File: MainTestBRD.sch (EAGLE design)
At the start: 24 parts, among them J1 COMPUTER-PERIPHERAL-POWERVERT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, U1 ATMEGA128-SMD

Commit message: intermedate variant
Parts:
- R1, R2: value (none) -> 1.8k; device mbed-rlcq:R0.125W -> SparkFun-Resistors:1.8KOHM1/10W1%(0603)
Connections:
- net N$13 renamed RESET
- net LED1: now also R1.2; no longer R1.P$1
- net LED2: now also R2.2; no longer R2.P$1
- net N$2: now also R2.1; no longer R2.P$2
- net N$5: now also R1.1; no longer R1.P$2
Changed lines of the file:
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@@
 <part name="U1" library="SparkFun-DigitalIC" deviceset="ATMEGA128" device="-SMD"/>
 <part name="GND1" library="mbed-power" deviceset="GND" device=""/>
-<part name="R1" library="mbed-rlcq" deviceset="R" device="0.125W"/>
-<part name="R2" library="mbed-rlcq" deviceset="R" device="0.125W"/>
 <part name="GND3" library="mbed-power" deviceset="GND" device=""/>
 <part name="GND4" library="mbed-power" deviceset="GND" device=""/>
@@
 <part name="C9" library="SparkFun-Capacitors" deviceset="10UF-6.3V-20%(1206)" device="" value="10pF"/>
 <part name="C10" library="SparkFun-Capacitors" deviceset="10UF-6.3V-20%(1206)" device="" value="10pF"/>
+<part name="R1" library="SparkFun-Resistors" deviceset="1.8KOHM1/10W1%(0603)" device="" value="1.8k"/>
+<part name="R2" library="SparkFun-Resistors" deviceset="1.8KOHM1/10W1%(0603)" device="" value="1.8k"/>
 </parts>
 <sheets>
@@
 <instance part="U1" gate="G$1" x="177.8" y="71.12"/>
 <instance part="GND1" gate="1" x="55.88" y="12.7"/>
-<instance part="R1" gate="G$1" x="81.28" y="50.8"/>
-<instance part="R2" gate="G$1" x="81.28" y="33.02"/>
 <instance part="GND3" gate="1" x="205.74" y="7.62"/>
 <instance part="GND4" gate="1" x="134.62" y="91.44"/>
@@
 <instance part="C9" gate="G$1" x="236.22" y="86.36" rot="R90"/>
 <instance part="C10" gate="G$1" x="236.22" y="96.52" rot="R90"/>
+<instance part="R1" gate="G$1" x="81.28" y="50.8" rot="R180"/>
+<instance part="R2" gate="G$1" x="81.28" y="33.02" rot="R180"/>
 </instances>
 <busses>
@@
 <segment>
 <pinref part="U$1" gate="G$1" pin="PIO5"/>
-<pinref part="R1" gate="G$1" pin="P$1"/>
 <wire x1="76.2" y1="50.8" x2="50.8" y2="50.8" width="0.1524" layer="91"/>
+<pinref part="R1" gate="G$1" pin="2"/>
 </segment>
 </net>
 <net name="N$5" class="0">
 <segment>
-<pinref part="R1" gate="G$1" pin="P$2"/>
 <wire x1="86.36" y1="50.8" x2="88.9" y2="50.8" width="0.1524" layer="91"/>
 <pinref part="LED1" gate="G$1" pin="C"/>
+<pinref part="R1" gate="G$1" pin="1"/>
 </segment>
 </net>
 <net name="N$2" class="0">
 <segment>
-<pinref part="R2" gate="G$1" pin="P$2"/>
 <wire x1="88.9" y1="33.02" x2="86.36" y2="33.02" width="0.1524" layer="91"/>
 <pinref part="LED2" gate="G$1" pin="C"/>
+<pinref part="R2" gate="G$1" pin="1"/>
 </segment>
 </net>
@@
 <wire x1="50.8" y1="43.18" x2="53.34" y2="43.18" width="0.1524" layer="91"/>
 <wire x1="53.34" y1="43.18" x2="53.34" y2="33.02" width="0.1524" layer="91"/>
-<pinref part="R2" gate="G$1" pin="P$1"/>
 <wire x1="53.34" y1="33.02" x2="76.2" y2="33.02" width="0.1524" layer="91"/>
+<pinref part="R2" gate="G$1" pin="2"/>
 </segment>
 </net>
@@
 </segment>
 </net>
-<net name="N$13" class="0">
+<net name="RESET" class="0">
 <segment>
 <pinref part="S1" gate="S" pin="4"/>

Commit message: other pinouts
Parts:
- removed J1: COMPUTER-PERIPHERAL-POWERVERTICAL, SparkFun-Connectors:COMPUTER-PERIPHERAL-POWERVERTICAL
- removed U$2: JTAGICE3-CONNECTOR100MIL-SMD, con-jtagice3:JTAGICE3-CONNECTOR100MIL-SMD
- added JP1: M05X2PTH, SparkFun-Connectors:M05X2PTH
- added U$3: JTAGICE3-CONNECTOR50MIL-THT, con-jtagice3:JTAGICE3-CONNECTOR50MIL-THT
- added U2: (no value), SparkFun-Connectors:USB-AB
- R3: device SparkFun-Resistors:1.8KOHM1/10W1%(0603) -> SparkFun-Resistors:3.3KOHM1/10W1%(0603)
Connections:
- new net N$10: JP1.10, U1.PE4
- new net N$11: JP1.8, U1.PE3
- new net N$12: JP1.6, U1.PE2
- new net N$13: JP1.4, U1.PE1(TXD)
- new net N$14: JP1.2, U1.PE0(RXD)
- new net N$15: JP1.9, U1.PE5
- new net N$16: JP1.7, U1.PE6
- new net N$17: JP1.5, U1.PE7
- new net N$3: R3.1, U1.PD3
- net BT_RX: no longer R3.1, U1.PD3
- net GND: now also JP1.3, U$3.GND@0, U$3.GND@1, U2.GND; no longer J1.GND
- net PF4: now also U$3.TCK; no longer U$2.TCK
- net PF5: now also U$3.TMS; no longer U$2.TMS
- net PF6: now also U$3.TDO; no longer U$2.TDO
- net PF7: now also U$3.TDI; no longer U$2.TDI
- net VCC: now also JP1.1, U$3.VTG, U2.VBUS; no longer J1.5V, U$2.VTG
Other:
- moved on the sheet: LED1, LED2, R1, R2, R3

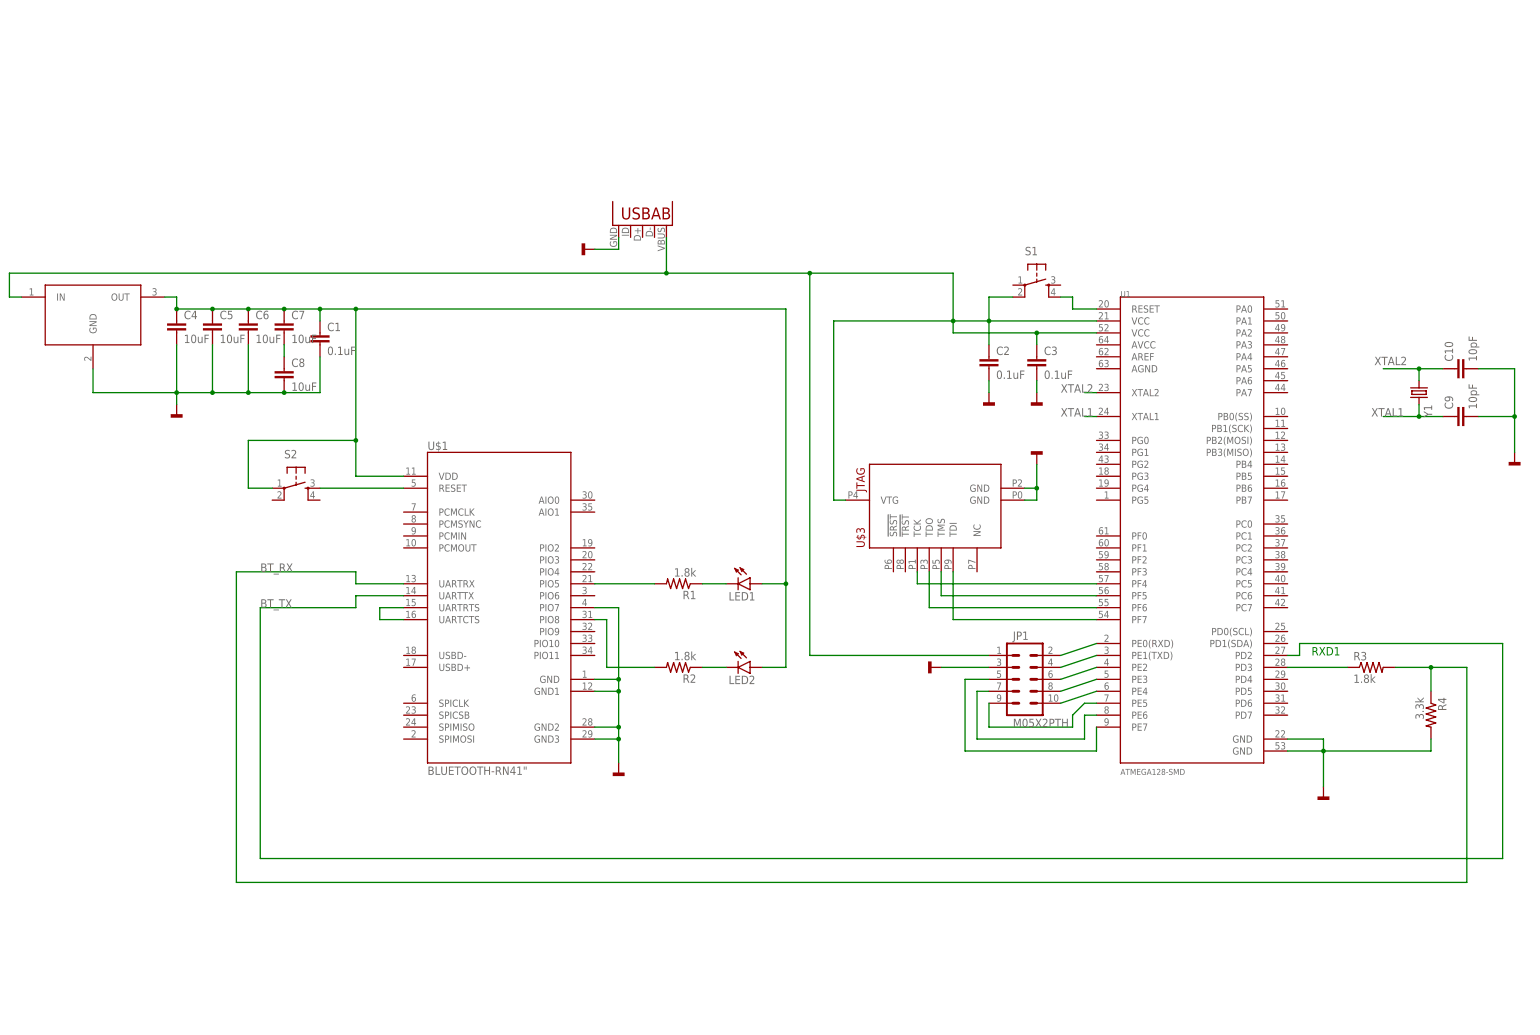
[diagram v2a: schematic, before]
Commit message: additional pin outs added
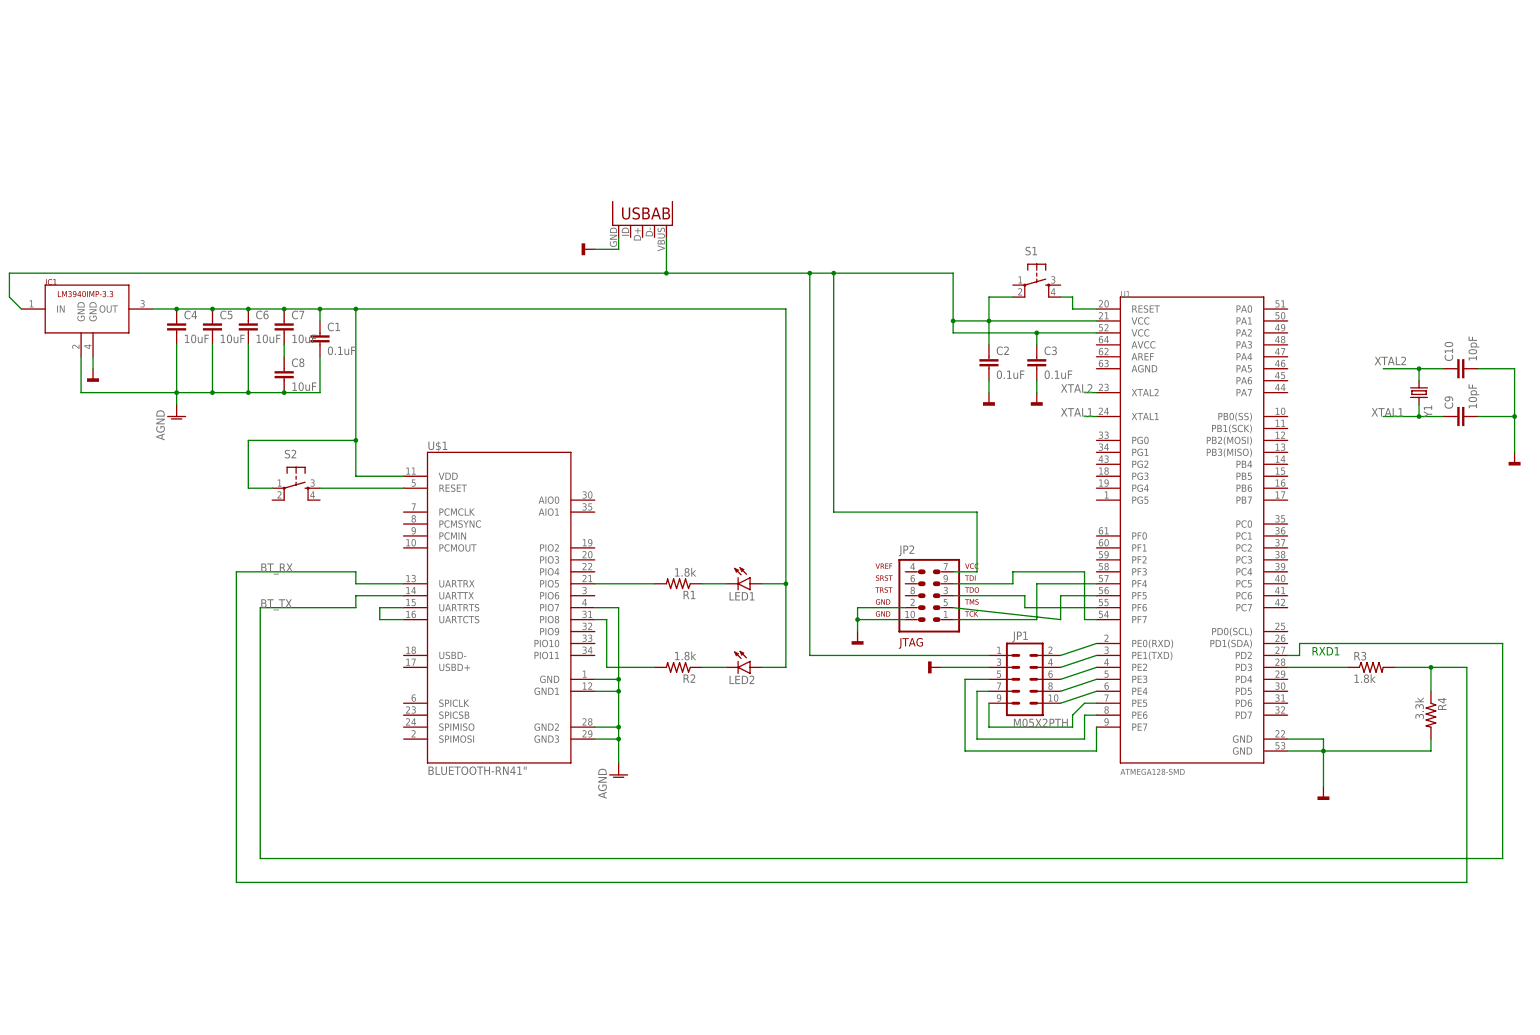
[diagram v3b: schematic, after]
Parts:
- removed IT1: LM3940IT-3.3, LM3940:LM3940IT-3.3
- removed U$3: JTAGICE3-CONNECTOR50MIL-THT, con-jtagice3:JTAGICE3-CONNECTOR50MIL-THT
- added IC1: LM3940IMP-3.3, mylib:LM3940IMP-3.3
- added JP2: AVR-JTAG-10, atmel:AVR-JTAG-10
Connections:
- removed net PF4: U$3.TCK, U1.PF4
- removed net PF5: U$3.TMS, U1.PF5
- removed net PF6: U$3.TDO, U1.PF6
- removed net PF7: U$3.TDI, U1.PF7
- new net AGND: C1.2, C4.2, C5.2, C6.2, C8.2, IC1.GND@1, U$1.GND, U$1.GND1, U$1.GND2, U$1.GND3, U$1.PIO7
- new net N$18: JP2.3, U1.PF6
- new net N$19: JP2.9, U1.PF7
- new net N$6: JP2.1, U1.PF4
- new net N$9: JP2.5, U1.PF5
- net GND: now also IC1.GND@2, JP2.10, JP2.2; no longer C1.2, C4.2, C5.2, C6.2, C8.2, IT1.GND, U$1.GND, U$1.GND1, U$1.GND2, U$1.GND3, U$1.PIO7, U$3.GND@0, U$3.GND@1
- net VCC: now also IC1.IN, JP2.7; no longer IT1.IN, U$3.VTG
- net VDD: now also IC1.OUT; no longer IT1.OUT

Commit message: new power led
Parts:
- added LED3: (no value), SparkFun-LED:LED1206
- added R5: 1.8k, SparkFun-Resistors:1.8KOHM1/10W1%(0603)
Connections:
- new net N$20: LED3.C, R5.1
- net GND: now also R5.2
- net VCC: now also LED3.A
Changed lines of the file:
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@@
 <part name="GND1" library="mbed-power" deviceset="GND" device=""/>
 <part name="JP2" library="atmel" deviceset="AVR-JTAG-10" device=""/>
+<part name="LED3" library="SparkFun-LED" deviceset="LED" device="1206"/>
+<part name="GND6" library="mbed-power" deviceset="GND" device=""/>
+<part name="R5" library="SparkFun-Resistors" deviceset="1.8KOHM1/10W1%(0603)" device="" value="1.8k"/>
 </parts>
 <sheets>
@@
 <instance part="GND1" gate="1" x="-55.88" y="96.52"/>
 <instance part="JP2" gate="G$1" x="121.92" y="48.26"/>
+<instance part="LED3" gate="G$1" x="83.82" y="121.92" rot="R180"/>
+<instance part="GND6" gate="1" x="83.82" y="137.16" rot="R180"/>
+<instance part="R5" gate="G$1" x="83.82" y="132.08" rot="R90"/>
 </instances>
 <busses>
@@
 <pinref part="GND1" gate="1" pin="GND"/>
 <wire x1="-55.88" y1="96.52" x2="-55.88" y2="99.06" width="0.1524" layer="91"/>
+</segment>
+<segment>
+<pinref part="GND6" gate="1" pin="GND"/>
+<pinref part="R5" gate="G$1" pin="2"/>
 </segment>
 </net>
@@
 <wire x1="-73.66" y1="116.84" x2="-73.66" y2="111.76" width="0.1524" layer="91"/>
 <wire x1="-73.66" y1="111.76" x2="-71.12" y2="109.22" width="0.1524" layer="91"/>
-<wire x1="66.04" y1="116.84" x2="96.52" y2="116.84" width="0.1524" layer="91"/>
+<wire x1="66.04" y1="116.84" x2="83.82" y2="116.84" width="0.1524" layer="91"/>
+<wire x1="83.82" y1="116.84" x2="96.52" y2="116.84" width="0.1524" layer="91"/>
 <wire x1="96.52" y1="116.84" x2="101.6" y2="116.84" width="0.1524" layer="91"/>
 <wire x1="101.6" y1="116.84" x2="127" y2="116.84" width="0.1524" layer="91"/>
@@
 <wire x1="132.08" y1="66.04" x2="101.6" y2="66.04" width="0.1524" layer="91"/>
 <junction x="101.6" y="116.84"/>
+<pinref part="LED3" gate="G$1" pin="A"/>
+<wire x1="83.82" y1="119.38" x2="83.82" y2="116.84" width="0.1524" layer="91"/>
+<junction x="83.82" y="116.84"/>
 </segment>
 </net>
@@
 </segment>
 </net>
+<net name="N$20" class="0">
+<segment>
+<pinref part="LED3" gate="G$1" pin="C"/>
+<pinref part="R5" gate="G$1" pin="1"/>
+</segment>
+</net>

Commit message: new usb connector
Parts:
- removed U2: (no value), SparkFun-Connectors:USB-AB
- added JP4: USB-B, SparkFun-Connectors:USBPTH
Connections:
- net GND: now also JP4.GND; no longer U2.GND
- net VCC: now also JP4.VBUS; no longer U2.VBUS
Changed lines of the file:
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@@
 <part name="R1" library="SparkFun-Resistors" deviceset="1.8KOHM1/10W1%(0603)" device="" value="1.8k"/>
 <part name="R2" library="SparkFun-Resistors" deviceset="1.8KOHM1/10W1%(0603)" device="" value="1.8k"/>
-<part name="U2" library="SparkFun-Connectors" deviceset="USB-AB" device=""/>
 <part name="GND8" library="mbed-power" deviceset="GND" device=""/>
 <part name="R3" library="SparkFun-Resistors" deviceset="3.3KOHM1/10W1%(0603)" device="" value="1.8k"/>
@@
 <part name="GND6" library="mbed-power" deviceset="GND" device=""/>
 <part name="R5" library="SparkFun-Resistors" deviceset="1.8KOHM1/10W1%(0603)" device="" value="1.8k"/>
+<part name="JP4" library="SparkFun-Connectors" deviceset="USB" device="PTH" value="USB-B"/>
 </parts>
 <sheets>
@@
 <instance part="LED2" gate="G$1" x="83.82" y="33.02" rot="R270"/>
 <instance part="S2" gate="S" x="-12.7" y="71.12"/>
-<instance part="GND2" gate="1" x="50.8" y="121.92" rot="R270"/>
+<instance part="GND2" gate="1" x="63.5" y="121.92" rot="R90"/>
 <instance part="Y1" gate="G$1" x="226.06" y="91.44" rot="R270"/>
 <instance part="GND7" gate="1" x="246.38" y="78.74"/>
@@
 <instance part="R1" gate="G$1" x="68.58" y="50.8" rot="R180"/>
 <instance part="R2" gate="G$1" x="68.58" y="33.02" rot="R180"/>
-<instance part="U2" gate="G$1" x="60.96" y="129.54" rot="R90"/>
 <instance part="GND8" gate="1" x="106.68" y="40.64"/>
 <instance part="R3" gate="G$1" x="215.9" y="33.02"/>
@@
 <instance part="GND6" gate="1" x="83.82" y="137.16" rot="R180"/>
 <instance part="R5" gate="G$1" x="83.82" y="132.08" rot="R90"/>
+<instance part="JP4" gate="G$1" x="60.96" y="127" rot="R90"/>
 </instances>
 <busses>
@@
 </segment>
 <segment>
-<wire x1="55.88" y1="121.92" x2="50.8" y2="121.92" width="0.1524" layer="91"/>
-<pinref part="GND2" gate="1" pin="GND"/>
-<pinref part="U2" gate="G$1" pin="GND"/>
-<wire x1="55.88" y1="121.92" x2="55.88" y2="124.46" width="0.1524" layer="91"/>
-</segment>
-<segment>
 <wire x1="238.76" y1="96.52" x2="246.38" y2="96.52" width="0.1524" layer="91"/>
 <pinref part="GND7" gate="1" pin="GND"/>
@@
 <pinref part="GND6" gate="1" pin="GND"/>
 <pinref part="R5" gate="G$1" pin="2"/>
+</segment>
+<segment>
+<pinref part="GND2" gate="1" pin="GND"/>
+<wire x1="63.5" y1="121.92" x2="60.96" y2="124.46" width="0.1524" layer="91"/>
+<pinref part="JP4" gate="G$1" pin="GND"/>
 </segment>
 </net>
@@
 <wire x1="-73.66" y1="116.84" x2="-73.66" y2="111.76" width="0.1524" layer="91"/>
 <wire x1="-73.66" y1="111.76" x2="-71.12" y2="109.22" width="0.1524" layer="91"/>
-<wire x1="66.04" y1="116.84" x2="83.82" y2="116.84" width="0.1524" layer="91"/>
 <wire x1="83.82" y1="116.84" x2="96.52" y2="116.84" width="0.1524" layer="91"/>
 <wire x1="96.52" y1="116.84" x2="101.6" y2="116.84" width="0.1524" layer="91"/>
@@
 <wire x1="134.62" y1="111.76" x2="134.62" y2="106.68" width="0.1524" layer="91"/>
 <wire x1="127" y1="116.84" x2="127" y2="106.68" width="0.1524" layer="91"/>
-<wire x1="-73.66" y1="116.84" x2="66.04" y2="116.84" width="0.1524" layer="91"/>
-<junction x="66.04" y="116.84"/>
+<wire x1="-73.66" y1="116.84" x2="58.42" y2="116.84" width="0.1524" layer="91"/>
 <pinref part="C2" gate="G$1" pin="1"/>
 <pinref part="C3" gate="G$1" pin="1"/>
-<pinref part="U2" gate="G$1" pin="VBUS"/>
-<wire x1="66.04" y1="116.84" x2="66.04" y2="124.46" width="0.1524" layer="91"/>
 <junction x="96.52" y="116.84"/>
+<wire x1="58.42" y1="116.84" x2="83.82" y2="116.84" width="0.1524" layer="91"/>
 <wire x1="96.52" y1="116.84" x2="96.52" y2="35.56" width="0.1524" layer="91"/>
 <wire x1="96.52" y1="35.56" x2="134.62" y2="35.56" width="0.1524" layer="91"/>
@@
 <wire x1="83.82" y1="119.38" x2="83.82" y2="116.84" width="0.1524" layer="91"/>
 <junction x="83.82" y="116.84"/>
-</segment>
-</net>
+<wire x1="58.42" y1="124.46" x2="58.42" y2="116.84" width="0.1524" layer="91"/>
+<junction x="58.42" y="116.84"/>
+<pinref part="JP4" gate="G$1" pin="VBUS"/>
+</segment>
+</net>

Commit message: новая версия
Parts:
- removed LED1, LED2: (no value), SparkFun-LED:LED1206
- removed R1, R2: 1.8k, SparkFun-Resistors:1.8KOHM1/10W1%(0603)
- removed S2: (no value), SparkFun-Electromechanical:TAC_SWITCHPTH
- removed U1: ATMEGA128-SMD, SparkFun-DigitalIC:ATMEGA128-SMD
- added BAT1: (no value), special:BATTERY
- added BLUE, GREEN, RED: (no value), SparkFun-LED:LED1206
- added C11: 10uF, SparkFun-Capacitors:10UF-6.3V-20%(1206)
- added IC2: AT90CAN128, at90can128:AT90CAN128
- added R6, R7, R8: 330R, SparkFun-Resistors:1.8KOHM1/10W1%(0603)
- added U$2: (no value), microchip:RN4020
- added UF4001: (no value), diode:DIODE-DO41-7.6
- U$1: value BLUETOOTH-RN41" -> LM3622; device SparkFun-RF:BLUETOOTH-RN41" -> adafruit:LM3622
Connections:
- removed net BRESET: S2.3, U$1.RESET
- removed net LED1: R1.2, U$1.PIO5
- removed net LED2: R2.2, U$1.PIO8
- removed net N$15: JP1.9, U1.PE5
- removed net N$16: JP1.7, U1.PE6
- removed net N$17: JP1.5, U1.PE7
- removed net N$18: JP2.3, U1.PF6
- removed net N$19: JP2.9, U1.PF7
- removed net RESET: S1.4, U1.RESET
- new net BT_WAKE_HW: IC2.(SDA/INT1)PD1, U$2.WAKE_HW
- new net N$4: BLUE.C, R6.1
- new net N$7: R7.1, RED.C
- net AGND: now also BLUE.A, GREEN.A, RED.A, U$2.GND@1, U$2.GND@2, U$2.GND@3, U$2.GND@4; no longer U$1.GND, U$1.GND1, U$1.GND2, U$1.GND3, U$1.PIO7
- net BT_RX: now also U$2.UART_RX; no longer U$1.UARTRX
- net BT_TX: now also IC2.(RXD1/INT2)PD2, U$2.UART_TX; no longer U$1.UARTTX, U1.PD2
- net GND: now also C11.1, IC2.GND, IC2.GND_53; no longer U1.GND@22, U1.GND@53
- net N$1: now also R6.2, U$2.WS/PIO2/MOSI; no longer U$1.UARTCTS, U$1.UARTRTS
- net N$10: now also GREEN.C, R8.1; no longer JP1.10, U1.PE4
- net N$11: now also IC2.PF6(ADC6/TDO), JP2.3; no longer JP1.8, U1.PE3
- net N$12: now also IC2.PF7(ADC7/TDI), JP2.9; no longer JP1.6, U1.PE2
- net N$13: now also IC2.RESET, S1.4; no longer JP1.4, U1.PE1(TXD)
- net N$14: now also C11.2, JP4.VBUS, LED3.A, UF4001.A; no longer JP1.2, U1.PE0(RXD)
- net N$2: now also R8.2, U$2.PIO1/SCK; no longer LED2.C, R2.1
- net N$3: now also IC2.(TXD1/INT3)PD3; no longer U1.PD3
- net N$5: now also R7.2, U$2.MLDP_EV/PIO2/CS; no longer LED1.C, R1.1
- net N$6: now also IC2.PF4(ADC4/TCK); no longer U1.PF4
- net N$9: now also IC2.PF5(ADC5/TMS); no longer U1.PF5
- net VCC: now also IC2.VCC, IC2.VCC_52; no longer JP4.VBUS, LED3.A, U1.VCC@21, U1.VCC@52
- net VDD: now also U$2.VDD; no longer LED1.A, LED2.A, S2.1, U$1.VDD
- net XTAL1: now also IC2.XTAL1; no longer U1.XTAL1
- net XTAL2: now also IC2.XTAL2; no longer U1.XTAL2
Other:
- note removed: "RXD1"
- moved on the sheet: C2, C3, JP1, JP2, LED3, R3, R4, R5

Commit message: new implementation
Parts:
- removed BAT1: (no value), special:BATTERY
- added C12, C13: 0.1uF, SparkFun-Capacitors:10UF-6.3V-20%(1206)
- added JP3: M02LOCK, SparkFun-Connectors:M02LOCK
- added Q1: BC847BLT1SMD, transistor-npn:BC847BLT1SMD
- added Q2: BD139, transistor-npn:BD139
- added R1: 1.2k, SparkFun-Resistors:1.8KOHM1/10W1%(0603)
- added R2: 4.7k, SparkFun-Resistors:1.8KOHM1/10W1%(0603)
- added R9: 180, SparkFun-Resistors:1.8KOHM1/10W1%(0603)
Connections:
- new net N$15: C12.1, IC2.AREF
- new net N$16: IC2.PF0(ADC0), JP1.10
- new net N$17: C11.2, JP4.VBUS, LED3.A, R1.1, UF4001.A
- new net N$18: Q1.C, Q2.B, R9.1
- new net N$19: IC2.PF1(ADC1), JP1.8
- new net N$21: IC2.PF2(ADC2), JP1.6
- new net N$22: IC2.PF3(ADC3), JP1.4
- net GND: now also C12.2, C13.2, IC2.GND(A), JP3.2, Q1.E, Q2.E, R2.1
- net N$14: now also Q1.B, R1.2, R2.2; no longer C11.2, JP4.VBUS, LED3.A, UF4001.A
- net VCC: now also C13.1, IC2.AVCC, JP3.1, Q2.C, R9.2, UF4001.C
- net VDD: now also JP1.5
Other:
- moved on the sheet: C11, JP1, LED3, R5, UF4001
